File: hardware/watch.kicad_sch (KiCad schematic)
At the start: 29 parts, among them J1 Debug, J2 RTC_CALIB, Q1 BC846, SW1 MODE, SW2 ALARM, SW3 LIGHT, U1 STM32L053C8Ux, U2 LCD, Y1 32.768kHz

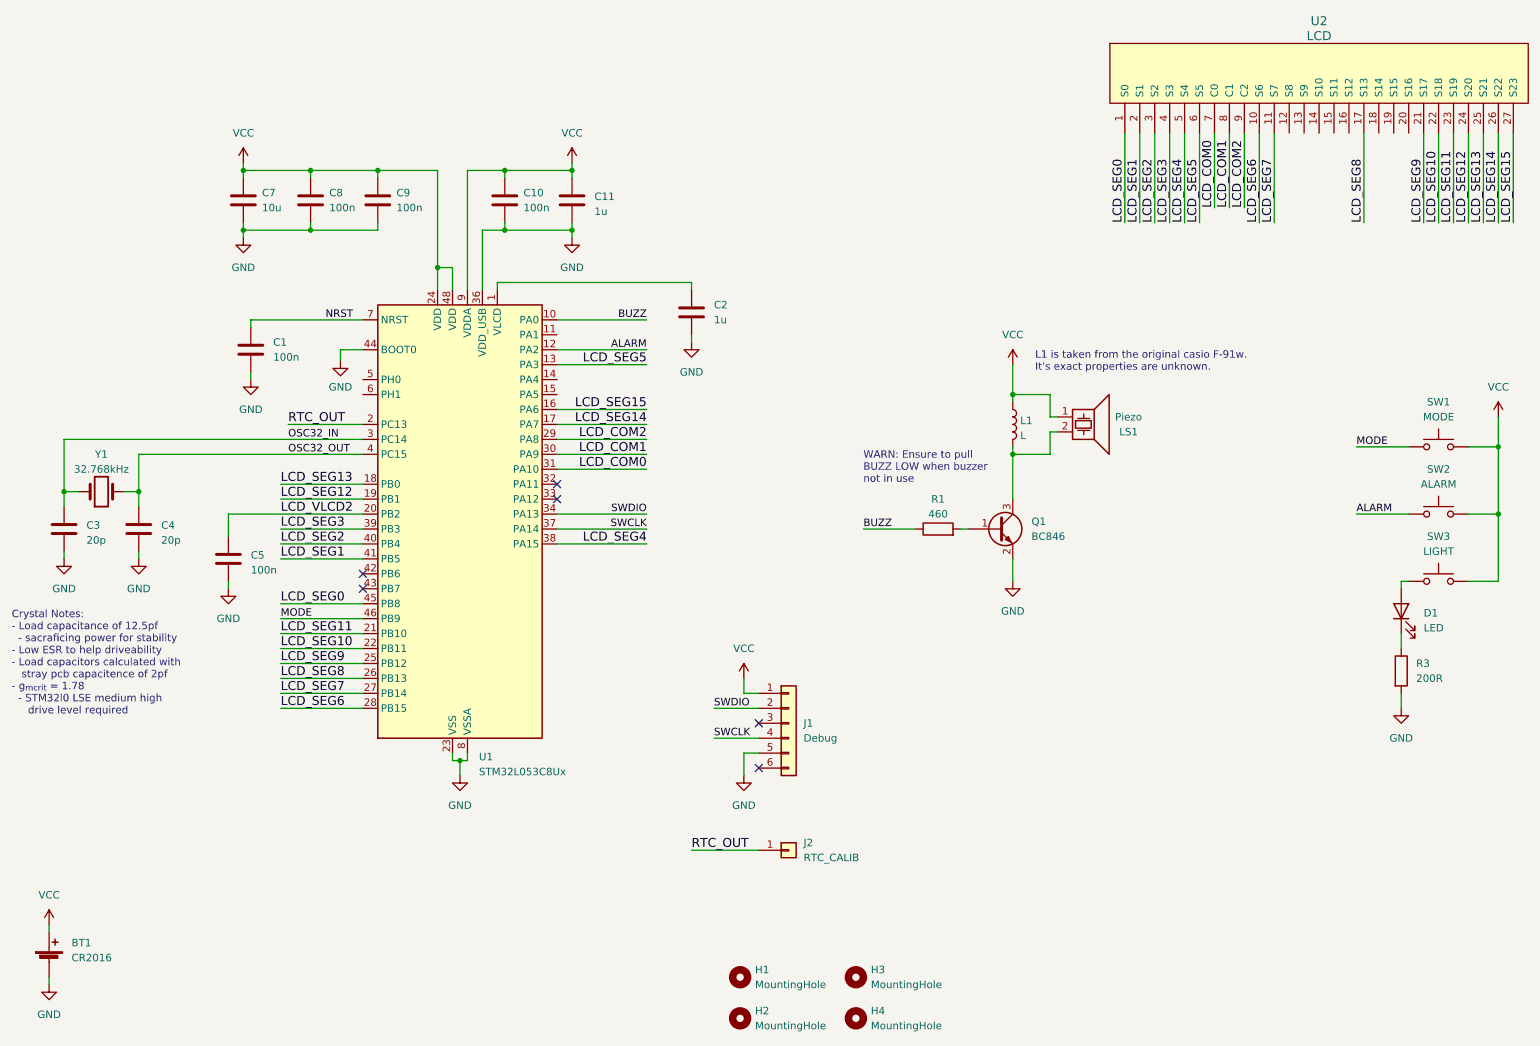
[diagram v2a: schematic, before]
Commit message: Move to MSP430FR6972 based hardware
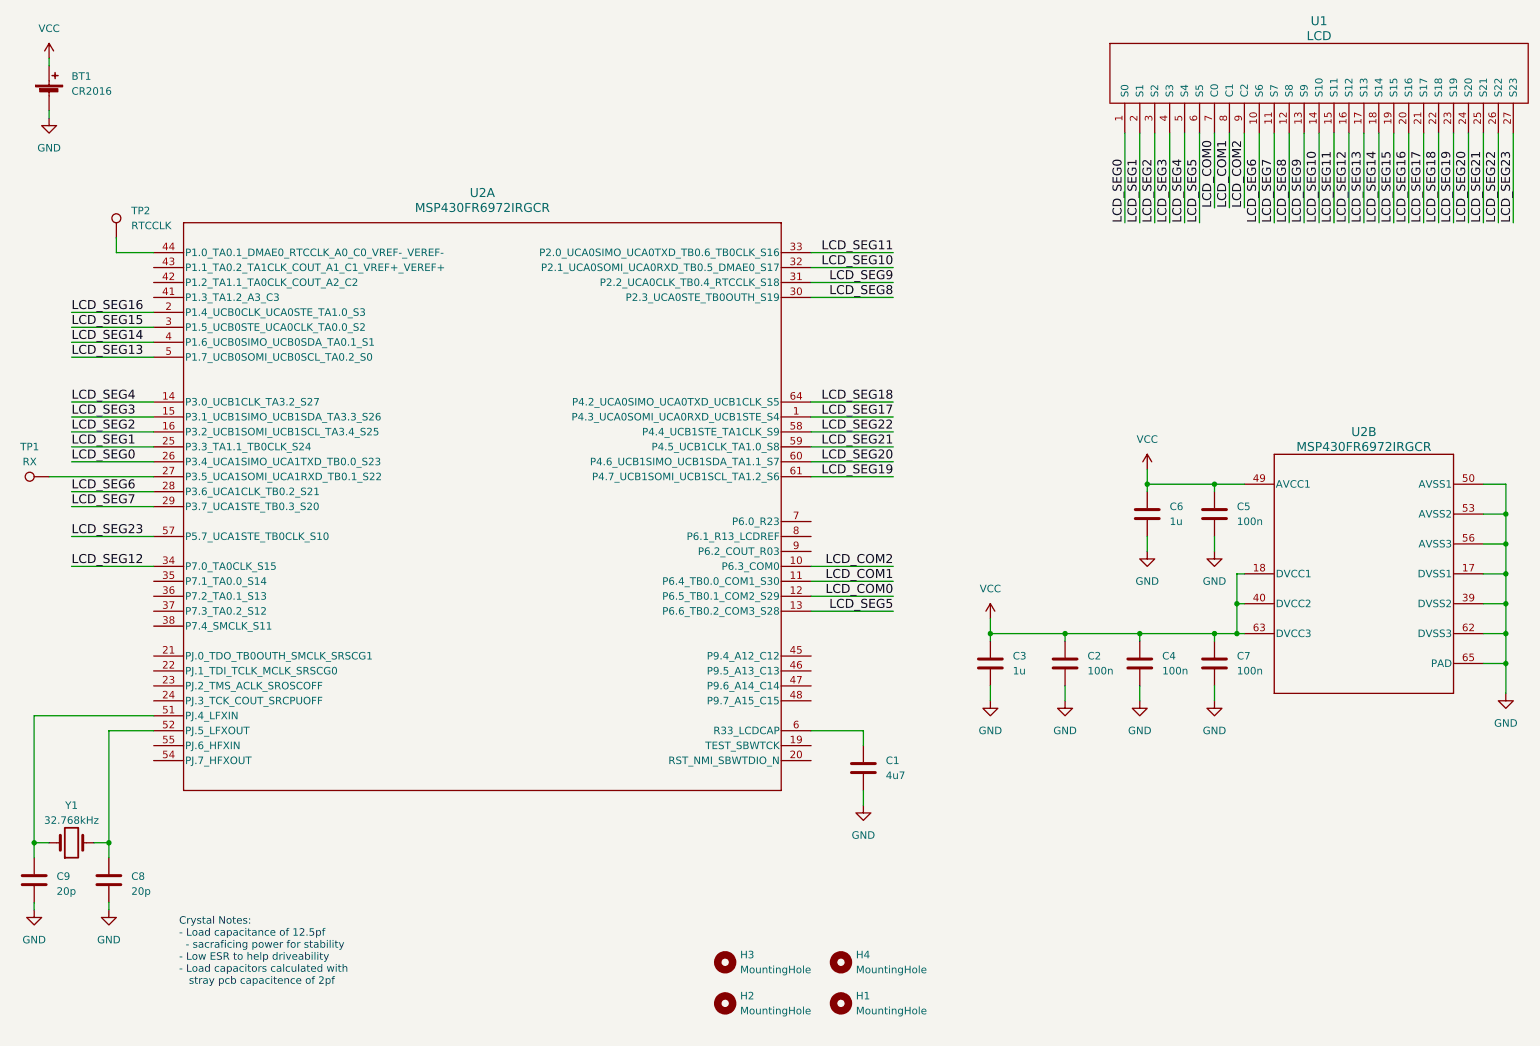
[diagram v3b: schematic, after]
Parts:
- removed C10, C8, C9: 100n, Capacitor_SMD:C_0402_1005Metric, symbol Device:C
- removed C11: 1u, Capacitor_SMD:C_0402_1005Metric, symbol Device:C
- removed D1: LED, LED_SMD:LED_1206_3216Metric, symbol Device:LED
- removed J1: Debug, Paw-Connect:Paw-Connect_RevB_TC2030-IDC-NL_2x03_P1.27mm_Vertical, symbol Connector_Generic:Conn_01x06
- removed J2: RTC_CALIB, TestPoint:TestPoint_Pad_1.0x1.0mm, symbol Connector_Generic:Conn_01x01
- removed L1: L, Inductor_SMD:L_1206_3216Metric, symbol Device:L
- removed LS1: Piezo, Watch:Buzzer, symbol Device:Speaker_Crystal
- removed Q1: BC846, Package_TO_SOT_SMD:SOT-523, symbol Transistor_BJT:BC846
- removed R1: 460, Resistor_SMD:R_0402_1005Metric, symbol Device:R
- removed R3: 200R, Resistor_SMD:R_0402_1005Metric, symbol Device:R
- removed SW1: MODE, Watch:Button, symbol Switch:SW_Push
- removed SW2: ALARM, Watch:Button, symbol Switch:SW_Push
- removed SW3: LIGHT, Watch:Button, symbol Switch:SW_Push
- removed U1: STM32L053C8Ux, Package_DFN_QFN:QFN-48-1EP_7x7mm_P0.5mm_EP5.6x5.6mm, symbol MCU_ST_STM32L0:STM32L053C8Ux
- added C3, C6: 1u, Capacitor_SMD:C_0402_1005Metric, symbol Device:C
- added C4: 100n, Capacitor_SMD:C_0402_1005Metric, symbol Device:C
- added TP1: RX, TestPoint:TestPoint_Pad_D1.0mm, symbol Connector:TestPoint
- added TP2: RTCCLK, TestPoint:TestPoint_Pad_D1.0mm, symbol Connector:TestPoint
- added U2: MSP430FR6972IRGCR, MSP430FR6972:RGC0064B_NV, symbol MSP430FR6972:MSP430FR6972IRGCR
- C1: value 100n -> 4u7
- C2: value 1u -> 100n
- C7: value 10u -> 100n
- renumbered C4 to C8, C3 to C9, H4 to H1, H1 to H3, H3 to H4, U2 to U1
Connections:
- net LCD_VLCD2 is gone; now on net VCC: C5.1
- net GND: now also C3.2, C4.2, C6.2, U2.17 (DVSS1), U2.39 (DVSS2), U2.50 (AVSS1), U2.53 (AVSS2), U2.56 (AVSS3), U2.62 (DVSS3), U2.65 (PAD)
- net LCD_COM0: now also U2.12 (P6.5_TB0.1_COM2_S29)
- net LCD_COM1: now also U2.11 (P6.4_TB0.0_COM1_S30)
- net LCD_COM2: now also U2.10 (P6.3_COM0)
- net LCD_SEG0: now also U2.26 (P3.4_UCA1SIMO_UCA1TXD_TB0.0_S23)
- net LCD_SEG1: now also U2.25 (P3.3_TA1.1_TB0CLK_S24)
- net LCD_SEG10: now also U1.14 (S10), U2.32 (P2.1_UCA0SOMI_UCA0RXD_TB0.5_DMAE0_S17); no longer U1.22 (S18)
- net LCD_SEG11: now also U1.15 (S11), U2.33 (P2.0_UCA0SIMO_UCA0TXD_TB0.6_TB0CLK_S16); no longer U1.23 (S19)
- net LCD_SEG12: now also U1.16 (S12), U2.34 (P7.0_TA0CLK_S15); no longer U1.24 (S20)
- net LCD_SEG13: now also U1.17 (S13), U2.5 (P1.7_UCB0SOMI_UCB0SCL_TA0.2_S0); no longer U1.25 (S21)
- net LCD_SEG14: now also U1.18 (S14), U2.4 (P1.6_UCB0SIMO_UCB0SDA_TA0.1_S1); no longer U1.26 (S22)
- net LCD_SEG15: now also U1.19 (S15), U2.3 (P1.5_UCB0STE_UCA0CLK_TA0.0_S2); no longer U1.27 (S23)
- net LCD_SEG2: now also U2.16 (P3.2_UCB1SOMI_UCB1SCL_TA3.4_S25)
- net LCD_SEG3: now also U2.15 (P3.1_UCB1SIMO_UCB1SDA_TA3.3_S26)
- net LCD_SEG4: now also U2.14 (P3.0_UCB1CLK_TA3.2_S27)
- net LCD_SEG5: now also U2.13 (P6.6_TB0.2_COM3_S28)
- net LCD_SEG6: now also U2.28 (P3.6_UCA1CLK_TB0.2_S21)
- net LCD_SEG7: now also U2.29 (P3.7_UCA1STE_TB0.3_S20)
- net LCD_SEG8: now also U1.12 (S8), U2.30 (P2.3_UCA0STE_TB0OUTH_S19); no longer U1.17 (S13)
- net LCD_SEG9: now also U1.13 (S9), U2.31 (P2.2_UCA0CLK_TB0.4_RTCCLK_S18); no longer U1.21 (S17)
- net VCC: now also C2.1, C3.1, C4.1, C6.1, U2.18 (DVCC1), U2.40 (DVCC2), U2.49 (AVCC1), U2.63 (DVCC3)
- net LCD_SEG16: now reaches U1.20 (S16)
- net LCD_SEG16: now also U2.2 (P1.4_UCB0CLK_UCA0STE_TA1.0_S3)
- net NRST: no longer names the net of C1.1
- net NRST: now also U2.6 (R33_LCDCAP)
- net OSC32_IN: no longer names the net of C9.1, Y1.1
- net OSC32_IN: now also U2.51 (PJ.4_LFXIN)
- net OSC32_OUT: no longer names the net of C8.1, Y1.2
- net OSC32_OUT: now also U2.52 (PJ.5_LFXOUT)
- new net: TP2.1, U2.44 (P1.0_TA0.1_DMAE0_RTCCLK_A0_C0_VREF-_VEREF-)
- new net: TP1.1, U2.27 (P3.5_UCA1SOMI_UCA1RXD_TB0.1_S22)
- new net LCD_SEG17: U1.21 (S17), U2.1 (P4.3_UCA0SOMI_UCA0RXD_UCB1STE_S4)
- new net LCD_SEG18: U1.22 (S18), U2.64 (P4.2_UCA0SIMO_UCA0TXD_UCB1CLK_S5)
- new net LCD_SEG19: U1.23 (S19), U2.61 (P4.7_UCB1SOMI_UCB1SCL_TA1.2_S6)
- new net LCD_SEG20: U1.24 (S20), U2.60 (P4.6_UCB1SIMO_UCB1SDA_TA1.1_S7)
- new net LCD_SEG21: U1.25 (S21), U2.59 (P4.5_UCB1CLK_TA1.0_S8)
- new net LCD_SEG22: U1.26 (S22), U2.58 (P4.4_UCB1STE_TA1CLK_S9)
- new net LCD_SEG23: U1.27 (S23), U2.57 (P5.7_UCA1STE_TB0CLK_S10)
- no-connect marks 6 -> 0
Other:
- note added: "Crystal Notes: - Load capacitance of 12.5pf - sacraficing power for stability - Low ESR to help driveability - Load capacitors calculated with stray pcb capacitence of 2pf"
- note removed: "Crystal Notes: - Load capacitance of 12.5pf - sacraficing power for stability - Low ESR to help driveability - Load capacitors calculated with stray pcb capacitence of 2pf - g_{mcrit} = 1.78 - STM32l0 LSE medium high drive level required"
- note removed: "L1 is taken from the original casio F-91w. It's exact properties are unknown."
- note removed: "WARN: Ensure to pull BUZZ LOW when buzzer not in use"
- moved on the sheet: BT1, C8, C9, H1, H2, H3, H4, Y1
